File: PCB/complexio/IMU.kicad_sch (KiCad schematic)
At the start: 15 parts, among them J5 Conn_01x03_Pin, U1 MPU6050, U23 AP2112K-3.3

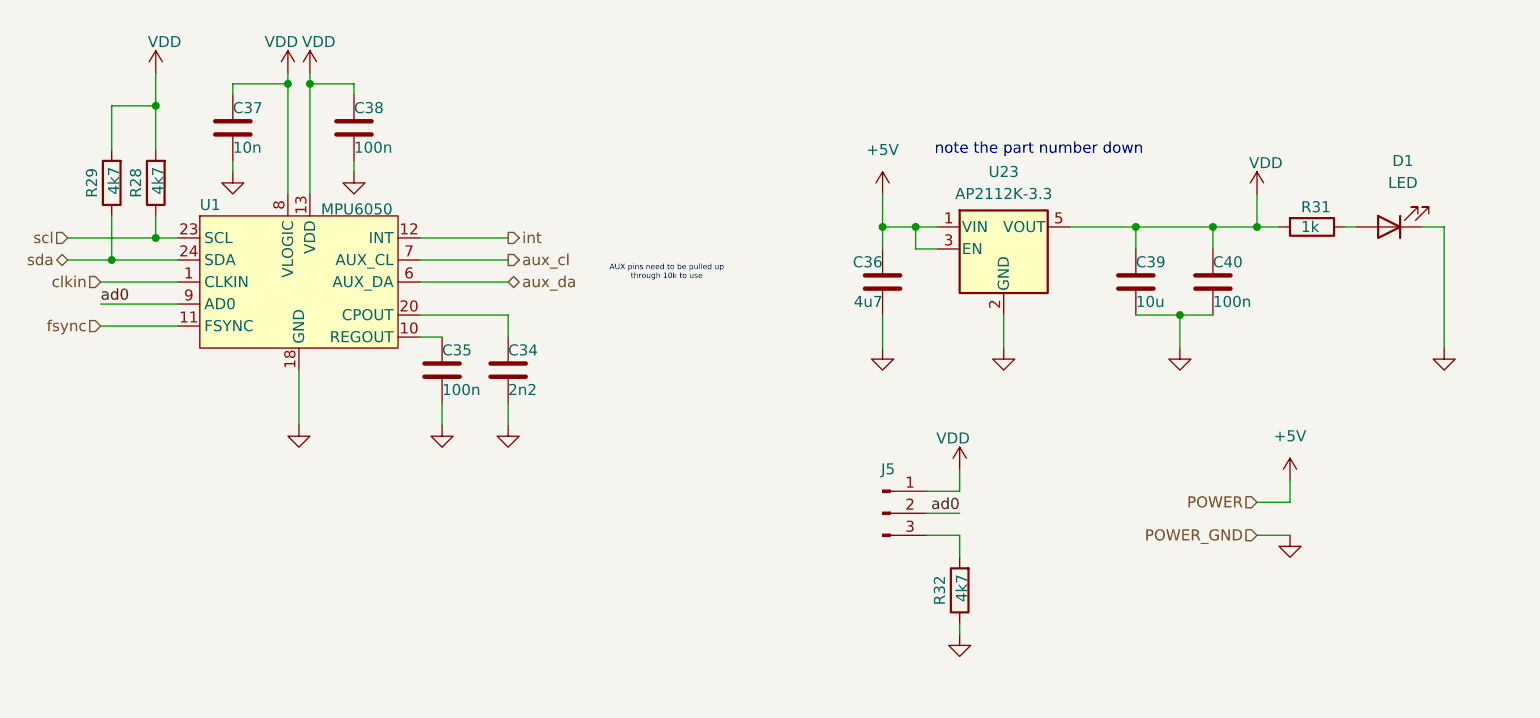
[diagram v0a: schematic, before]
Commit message: Advanced with schem & resolved main power problem
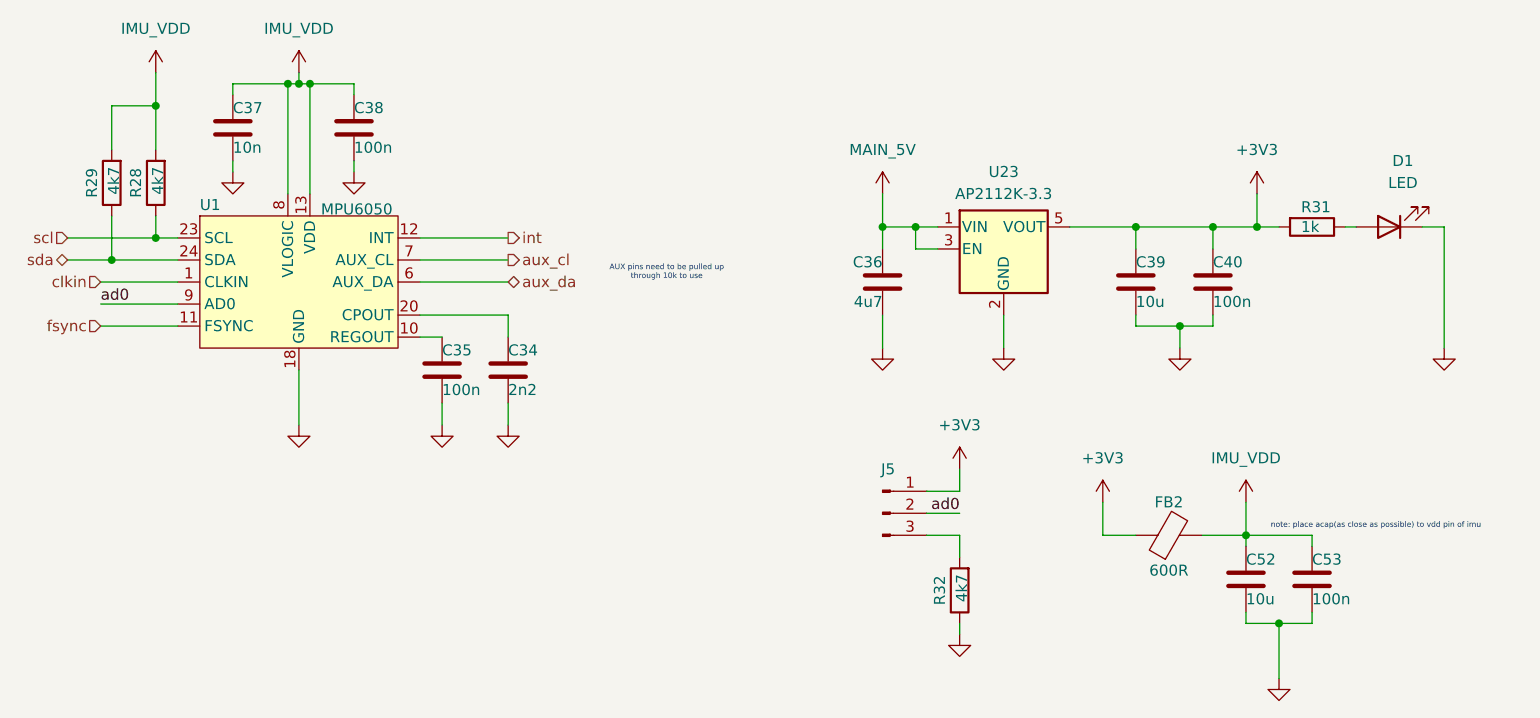
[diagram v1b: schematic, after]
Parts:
- added C52: 10u, Capacitor_SMD:C_0603_1608Metric, symbol Device:C
- added C53: 100n, Capacitor_SMD:C_0402_1005Metric, symbol Device:C
- added FB2: 600R, Inductor_SMD:L_0603_1608Metric, symbol Device:FerriteBead
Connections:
- net GND: now also C52.2, C53.2
- net +5V renamed MAIN_5V
- net VDD renamed IMU_VDD
- net IMU_VDD: now also C52.1, C53.1, FB2.2; no longer C39.1, C40.1, J5.1 (Pin_1), R31.2, U23.5 (VOUT)
- new net +3V3: C39.1, C40.1, FB2.1, J5.1 (Pin_1), R31.2, U23.5 (VOUT)
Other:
- note added: "note: place acap(as close as possible) to vdd pin of imu"
- note removed: "note the part number down"
